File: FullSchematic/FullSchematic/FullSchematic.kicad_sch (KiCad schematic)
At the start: 0 parts

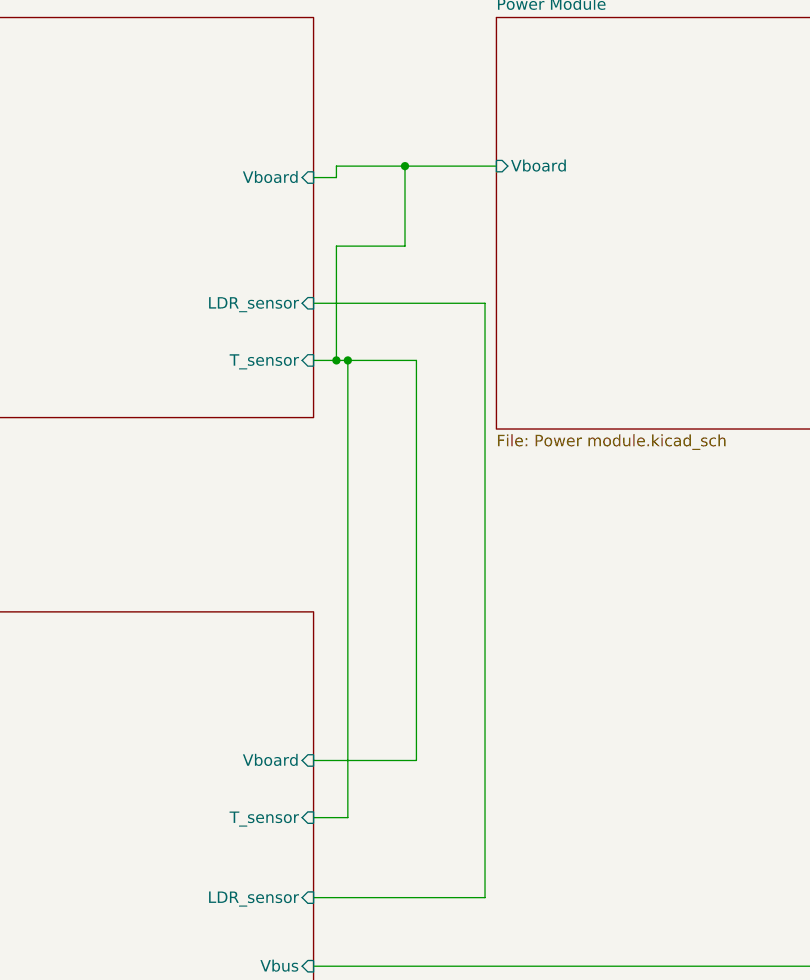
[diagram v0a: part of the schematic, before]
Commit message: updated schematics and footprints
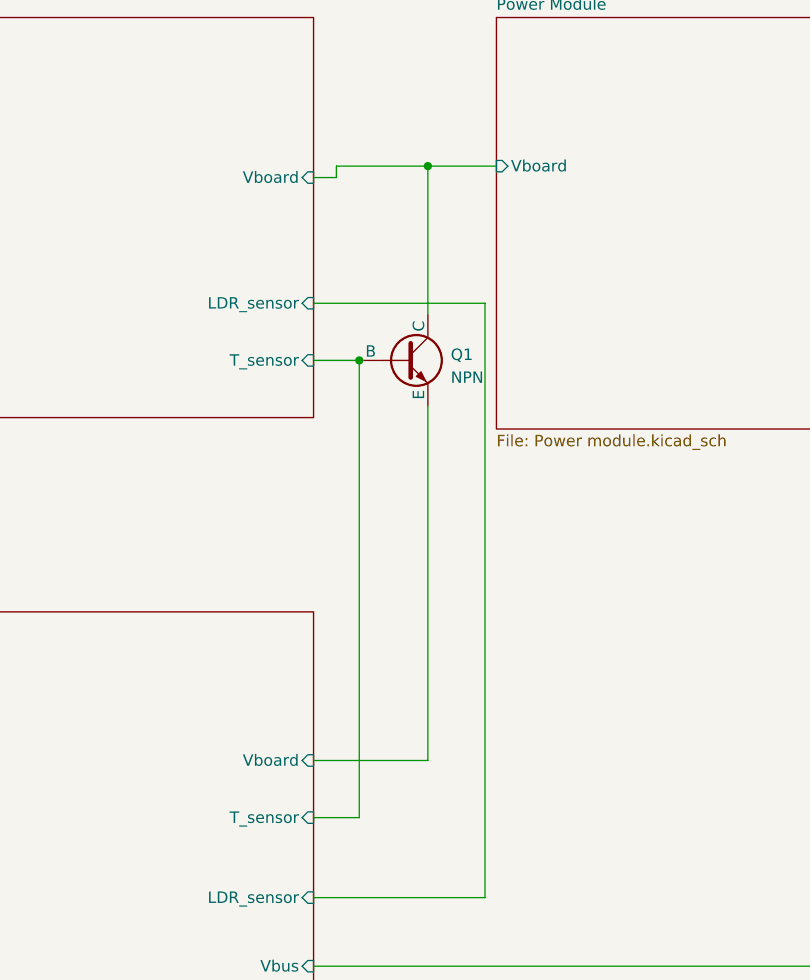
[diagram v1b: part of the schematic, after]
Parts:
- added Q1: NPN, Library:SOT95P237X112-3N, symbol Simulation_SPICE:NPN
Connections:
- net Microcontroller/T_sensor: now also Q1.2 (B)
- new net Microcontroller/Vboard: Q1.3 (E)
- new net Power Module/Vboard: Q1.1 (C)
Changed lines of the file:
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@@
     (comment 3 "Kudzi Kadzimu (KDZKUD001)")
   )
-  (junction (at 158.75 71.12) (diameter 0) (color 0 0 0 0)
+  (junction (at 167.64 49.53) (diameter 0) (color 0 0 0 0)
   )
-  (junction (at 157.48 71.12) (diameter 0) (color 0 0 0 0)
+  (junction (at 160.02 71.12) (diameter 0) (color 0 0 0 0)
   )
-  (junction (at 165.1 49.53) (diameter 0) (color 0 0 0 0)
+  (wire (pts (xy 154.94 71.12) (xy 160.02 71.12))
+    (stroke (width 0) (type default))
   )
   (wire (pts (xy 233.68 138.43) (xy 233.68 78.74))
@@
     (stroke (width 0) (type default))
   )
-  (wire (pts (xy 158.75 71.12) (xy 166.37 71.12))
-    (stroke (width 0) (type default))
-  )
-  (wire (pts (xy 157.48 58.42) (xy 157.48 71.12))
-    (stroke (width 0) (type default))
-  )
   (wire (pts (xy 173.99 64.77) (xy 173.99 130.81))
-    (stroke (width 0) (type default))
-  )
-  (wire (pts (xy 154.94 71.12) (xy 157.48 71.12))
     (stroke (width 0) (type default))
   )
@@
     (stroke (width 0) (type default))
   )
+  (wire (pts (xy 167.64 49.53) (xy 167.64 66.04))
+    (stroke (width 0) (type default))
+  )
   (wire (pts (xy 154.94 64.77) (xy 173.99 64.77))
     (stroke (width 0) (type default))
   )
-  (wire (pts (xy 157.48 49.53) (xy 165.1 49.53))
+  (wire (pts (xy 157.48 49.53) (xy 167.64 49.53))
     (stroke (width 0) (type default))
   )
-  (wire (pts (xy 165.1 58.42) (xy 157.48 58.42))
+  (wire (pts (xy 154.94 121.92) (xy 160.02 121.92))
     (stroke (width 0) (type default))
   )
-  (wire (pts (xy 158.75 121.92) (xy 154.94 121.92))
+  (wire (pts (xy 154.94 115.57) (xy 167.64 115.57))
     (stroke (width 0) (type default))
   )
-  (wire (pts (xy 154.94 115.57) (xy 166.37 115.57))
-    (stroke (width 0) (type default))
-  )
-  (wire (pts (xy 165.1 49.53) (xy 175.26 49.53))
-    (stroke (width 0) (type default))
-  )
-  (wire (pts (xy 166.37 71.12) (xy 166.37 115.57))
-    (stroke (width 0) (type default))
-  )
-  (wire (pts (xy 158.75 71.12) (xy 158.75 121.92))
+  (wire (pts (xy 167.64 49.53) (xy 175.26 49.53))
     (stroke (width 0) (type default))
   )
@@
     (stroke (width 0) (type default))
   )
-  (wire (pts (xy 157.48 71.12) (xy 158.75 71.12))
+  (wire (pts (xy 167.64 76.2) (xy 167.64 115.57))
+    (stroke (width 0) (type default))
+  )
+  (wire (pts (xy 160.02 71.12) (xy 160.02 121.92))
     (stroke (width 0) (type default))
   )
@@
     (stroke (width 0) (type default))
   )
-  (wire (pts (xy 165.1 49.53) (xy 165.1 58.42))
-    (stroke (width 0) (type default))
+  (symbol (lib_id "Simulation_SPICE:NPN") (at 165.1 71.12 0) (unit 1)
+    (in_bom yes) (on_board yes) (dnp no) (fields_autoplaced)
+    (property "Reference" "Q1" (at 170.18 70.485 0)
+      (effects (font (size 1.27 1.27)) (justify left))
+    )
+    (property "Value" "NPN" (at 170.18 73.025 0)
+      (effects (font (size 1.27 1.27)) (justify left))
+    )
+    (property "Footprint" "Library:SOT95P237X112-3N" (at 228.6 71.12 0)
+      (effects (font (size 1.27 1.27)) hide)
+    )
+    (property "Datasheet" "~" (at 228.6 71.12 0)
+      (effects (font (size 1.27 1.27)) hide)
+    )
+    (property "Sim.Device" "NPN" (at 165.1 71.12 0)
+      (effects (font (size 1.27 1.27)) hide)
+    )
+    (property "Sim.Type" "GUMMELPOON" (at 165.1 71.12 0)
+      (effects (font (size 1.27 1.27)) hide)
+    )
+    (property "Sim.Pins" "1=C 2=B 3=E" (at 165.1 71.12 0)
+      (effects (font (size 1.27 1.27)) hide)
+    )
+    (property "JLCPCB Part #" "C139719" (at 165.1 71.12 0)
+      (effects (font (size 1.27 1.27)) hide)
+    )
+    (property "Price" "0.1347" (at 165.1 71.12 0)
+      (effects (font (size 1.27 1.27)) hide)
+    )
+    (property "Price ( 1 board)" "0.1347" (at 165.1 71.12 0)
+      (effects (font (size 1.27 1.27)) hide)
+    )
+    (property "Price (5 boards)" "0.6735" (at 165.1 71.12 0)
+      (effects (font (size 1.27 1.27)) hide)
+    )
+    (pin "1")
+    (pin "2")
+    (pin "3")
+    (instances
+      (project "FullSchematic"
+        (path "/5dd86611-a33d-45ee-946c-01c599f30b12"
+          (reference "Q1") (unit 1)
+        )
+      )
+    )
   )
   (sheet (at 175.26 33.02) (size 95.25 45.72) (fields_autoplaced)

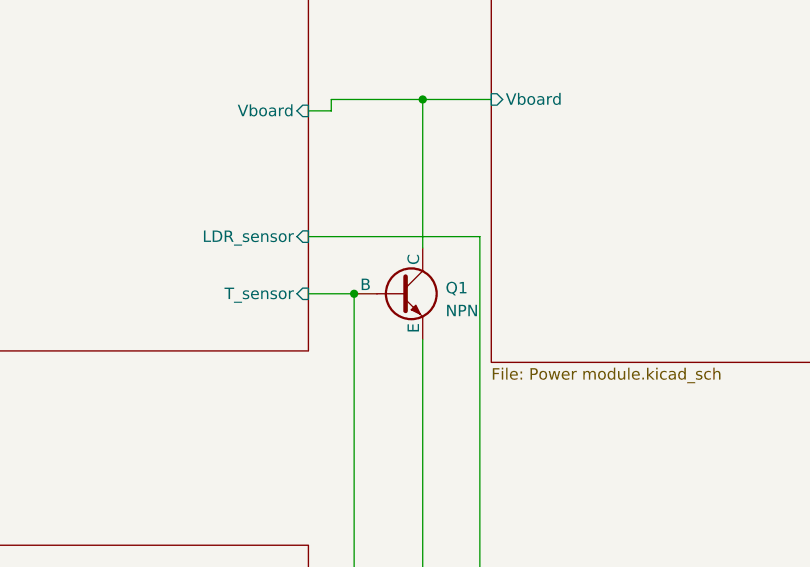
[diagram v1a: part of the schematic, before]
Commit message: updated schematic and footprints
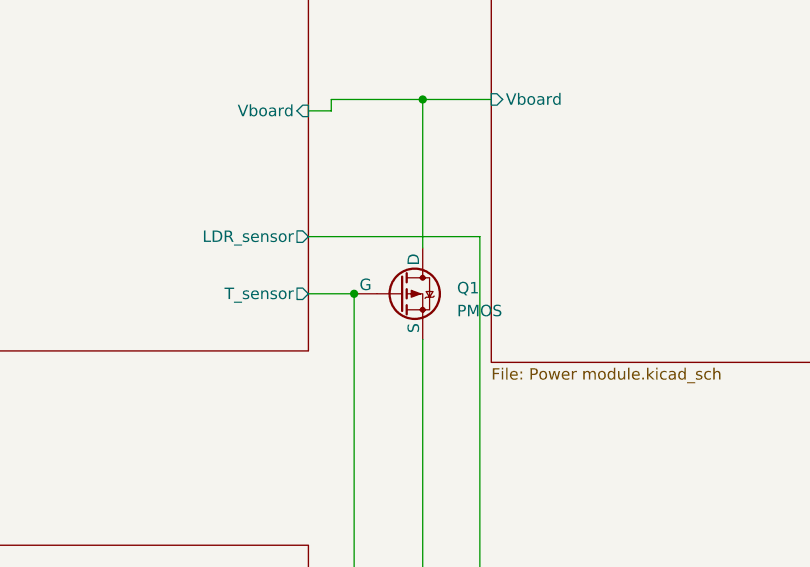
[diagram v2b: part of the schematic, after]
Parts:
- removed Q1: NPN, Library:SOT95P237X112-3N, symbol Simulation_SPICE:NPN
- added Q1: PMOS, Package_TO_SOT_THT:TO-3P-3_Vertical, symbol Simulation_SPICE:PMOS
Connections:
- net Microcontroller/T_sensor: now also Q1.2 (G)
- net Microcontroller/Vboard: now also Q1.3 (S)
- net Power Module/Vboard: now also Q1.1 (D)
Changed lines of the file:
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@@
   (junction (at 160.02 71.12) (diameter 0) (color 0 0 0 0)
-  )
-  (wire (pts (xy 154.94 71.12) (xy 160.02 71.12))
-    (stroke (width 0) (type default))
   )
   (wire (pts (xy 233.68 138.43) (xy 233.68 78.74))
@@
     (stroke (width 0) (type default))
   )
+  (wire (pts (xy 154.94 71.12) (xy 160.02 71.12))
+    (stroke (width 0) (type default))
+  )
   (wire (pts (xy 173.99 130.81) (xy 154.94 130.81))
     (stroke (width 0) (type default))
@@
     (stroke (width 0) (type default))
   )
+  (wire (pts (xy 154.94 138.43) (xy 233.68 138.43))
+    (stroke (width 0) (type default))
+  )
   (wire (pts (xy 160.02 71.12) (xy 160.02 121.92))
     (stroke (width 0) (type default))
   )
-  (wire (pts (xy 154.94 138.43) (xy 233.68 138.43))
-    (stroke (width 0) (type default))
-  )
-  (symbol (lib_id "Simulation_SPICE:NPN") (at 165.1 71.12 0) (unit 1)
+  (symbol (lib_id "Simulation_SPICE:PMOS") (at 165.1 71.12 0) (unit 1)
     (in_bom yes) (on_board yes) (dnp no) (fields_autoplaced)
-    (property "Reference" "Q1" (at 170.18 70.485 0)
+    (property "Reference" "Q1" (at 171.45 70.485 0)
       (effects (font (size 1.27 1.27)) (justify left))
     )
-    (property "Value" "NPN" (at 170.18 73.025 0)
+    (property "Value" "PMOS" (at 171.45 73.025 0)
       (effects (font (size 1.27 1.27)) (justify left))
     )
-    (property "Footprint" "Library:SOT95P237X112-3N" (at 228.6 71.12 0)
+    (property "Footprint" "Package_TO_SOT_THT:TO-3P-3_Vertical" (at 170.18 68.58 0)
       (effects (font (size 1.27 1.27)) hide)
     )
-    (property "Datasheet" "~" (at 228.6 71.12 0)
+    (property "Datasheet" "https://ngspice.sourceforge.io/docs/ngspice-manual.pdf" (at 165.1 83.82 0)
       (effects (font (size 1.27 1.27)) hide)
     )
-    (property "Sim.Device" "NPN" (at 165.1 71.12 0)
+    (property "Sim.Device" "PMOS" (at 165.1 88.265 0)
       (effects (font (size 1.27 1.27)) hide)
     )
-    (property "Sim.Type" "GUMMELPOON" (at 165.1 71.12 0)
+    (property "Sim.Type" "VDMOS" (at 165.1 90.17 0)
       (effects (font (size 1.27 1.27)) hide)
     )
-    (property "Sim.Pins" "1=C 2=B 3=E" (at 165.1 71.12 0)
-      (effects (font (size 1.27 1.27)) hide)
-    )
-    (property "JLCPCB Part #" "C139719" (at 165.1 71.12 0)
-      (effects (font (size 1.27 1.27)) hide)
-    )
-    (property "Price" "0.1347" (at 165.1 71.12 0)
-      (effects (font (size 1.27 1.27)) hide)
-    )
-    (property "Price ( 1 board)" "0.1347" (at 165.1 71.12 0)
-      (effects (font (size 1.27 1.27)) hide)
-    )
-    (property "Price (5 boards)" "0.6735" (at 165.1 71.12 0)
+    (property "Sim.Pins" "1=D 2=G 3=S" (at 165.1 86.36 0)
       (effects (font (size 1.27 1.27)) hide)
     )
@@
       (effects (font (size 1.27 1.27)) (justify right))
     )
-    (pin "LDR_sensor" input (at 154.94 64.77 0)
+    (pin "LDR_sensor" output (at 154.94 64.77 0)
       (effects (font (size 1.27 1.27)) (justify right))
     )
-    (pin "T_sensor" input (at 154.94 71.12 0)
+    (pin "T_sensor" output (at 154.94 71.12 0)
       (effects (font (size 1.27 1.27)) (justify right))
     )
